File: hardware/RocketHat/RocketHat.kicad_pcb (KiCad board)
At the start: 4 copper layers, 28 x 25 mm, 2 parts, among them J1 Conn_02x16_Top_Bottom, J2 Conn_02x16_Top_Bottom

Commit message: Rocket hat sensor libraries
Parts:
- added U1: BMP390, bmp390:10LGA_2X2X0p75_BOS, F.Cu at (152.5, 117.7)
- added U2: BMI088, Package_LGA:Bosch_LGA-16_4.5x3mm_P0.5mm_LayoutBorder7x1y_ClockwisePinNumbering, F.Cu at (152.7, 113.5)
- added U3: ADXL375BCCZ, adxl375:LGA_CC-14-1_ADI, F.Cu at (134.5, 115.8)
- added U4: CAM-M8C-0, CAM-M8C-0:CAM-M8C-0, F.Cu at (143.0, 103.5)

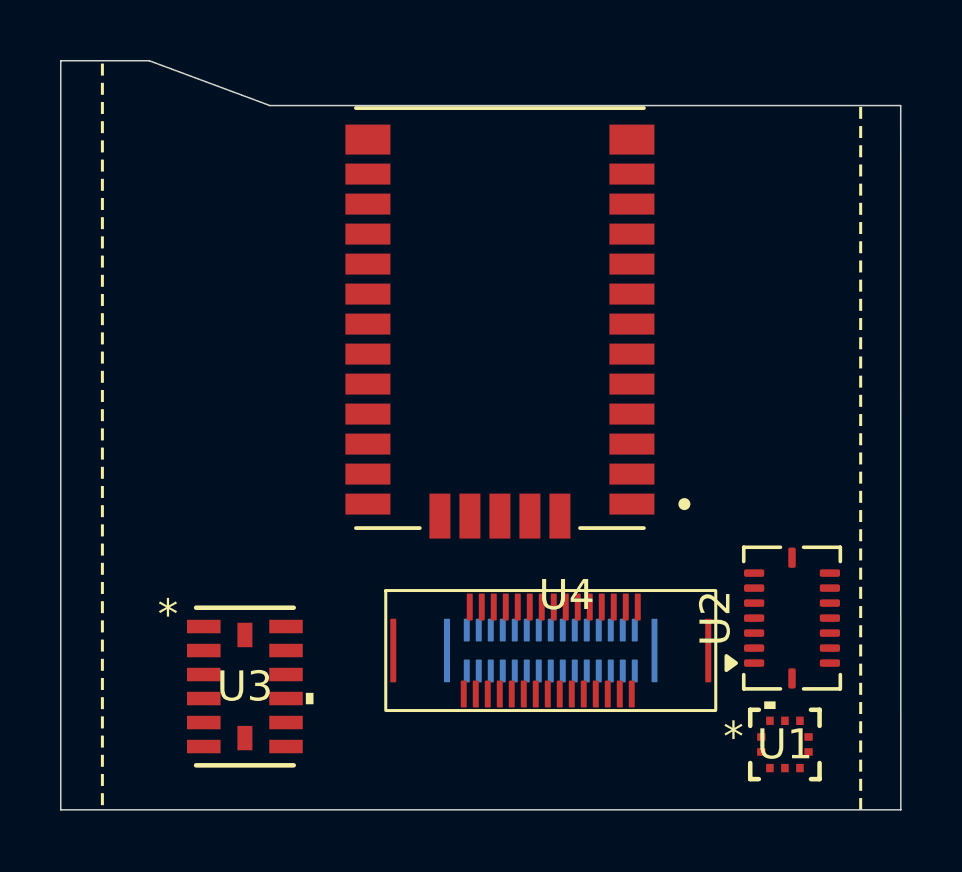
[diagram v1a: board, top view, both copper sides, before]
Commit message: Rocket Hat schematic done
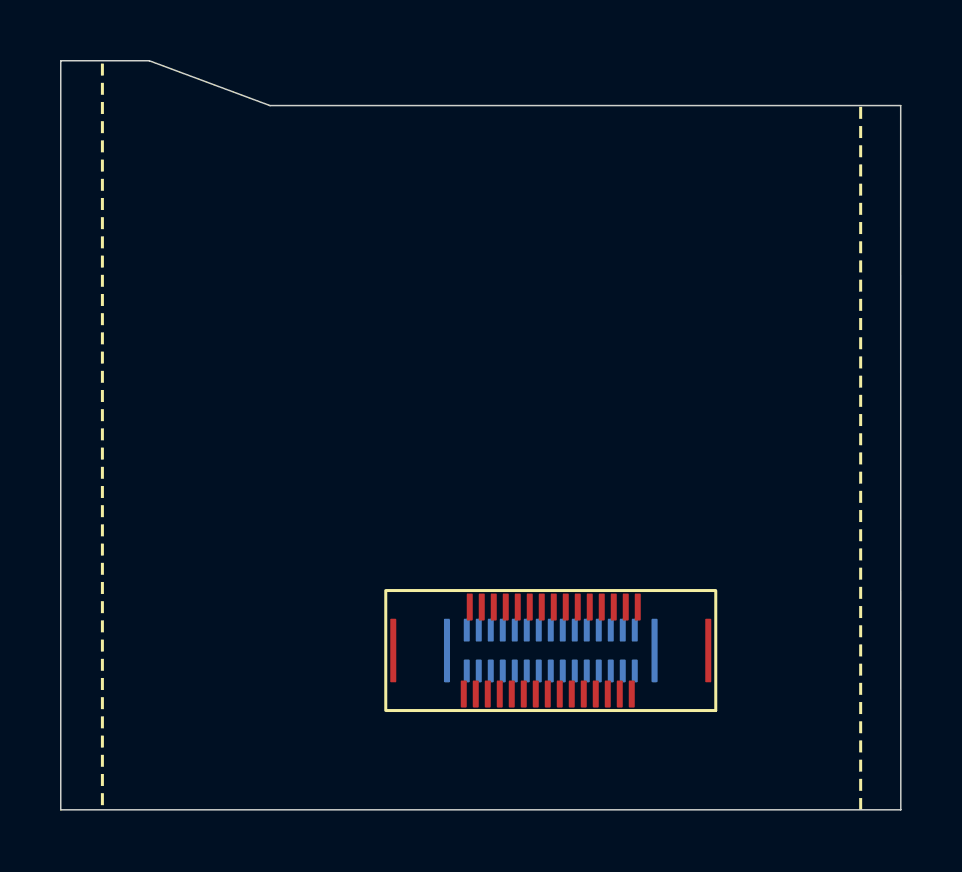
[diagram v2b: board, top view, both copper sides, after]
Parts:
- removed U1: BMP390, bmp390:10LGA_2X2X0p75_BOS
- removed U2: BMI088, Package_LGA:Bosch_LGA-16_4.5x3mm_P0.5mm_LayoutBorder7x1y_ClockwisePinNumbering
- removed U3: ADXL375BCCZ, adxl375:LGA_CC-14-1_ADI
- removed U4: CAM-M8C-0, CAM-M8C-0:CAM-M8C-0
- turned J2 to 180 degrees
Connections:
- J1 pad 17: CONN_16 -> CONN_16/I4
- J1 pad 18: CONN_17 -> CONN_17/I3
- J1 pad 19: CONN_18 -> CONN_18/I2
- J1 pad 20: CONN_19 -> CONN_19/I1
- J1 pad 21: CONN_20 -> CONN_20/I0
- J1 pad 22: CONN_21 -> CONN_21/RESP
- J2 pad 1: CONN_15 -> CONN_14
- J2 pad 10: CONN_24 -> CONN_5
- J2 pad 11: CONN_25 -> CONN_4
- J2 pad 12: CONN_26 -> CONN_3
- J2 pad 13: CONN_27 -> CONN_2
- J2 pad 14: CONN_28 -> CONN_1
- J2 pad 15: CONN_29 -> CONN_0
- J2 pad 16: CONN_0 -> CONN_29
- J2 pad 17: CONN_1 -> CONN_28
- J2 pad 18: CONN_2 -> CONN_27
- J2 pad 19: CONN_3 -> CONN_26
- J2 pad 2: CONN_16 -> CONN_13
- J2 pad 20: CONN_4 -> CONN_25
- J2 pad 21: CONN_5 -> CONN_24
- J2 pad 22: CONN_6 -> CONN_23
- J2 pad 23: CONN_7 -> CONN_22
- J2 pad 24: CONN_8 -> CONN_21
- J2 pad 25: CONN_9 -> CONN_20
- J2 pad 26: CONN_10 -> CONN_19
- J2 pad 27: CONN_11 -> CONN_18
- J2 pad 28: CONN_12 -> CONN_17
- J2 pad 29: CONN_13 -> CONN_16
- J2 pad 3: CONN_17 -> CONN_12
- J2 pad 30: CONN_14 -> CONN_15
- J2 pad 4: CONN_18 -> CONN_11
- J2 pad 5: CONN_19 -> CONN_10
- J2 pad 6: CONN_20 -> CONN_9
- J2 pad 7: CONN_21 -> CONN_8
- J2 pad 8: CONN_22 -> CONN_7
- J2 pad 9: CONN_23 -> CONN_6

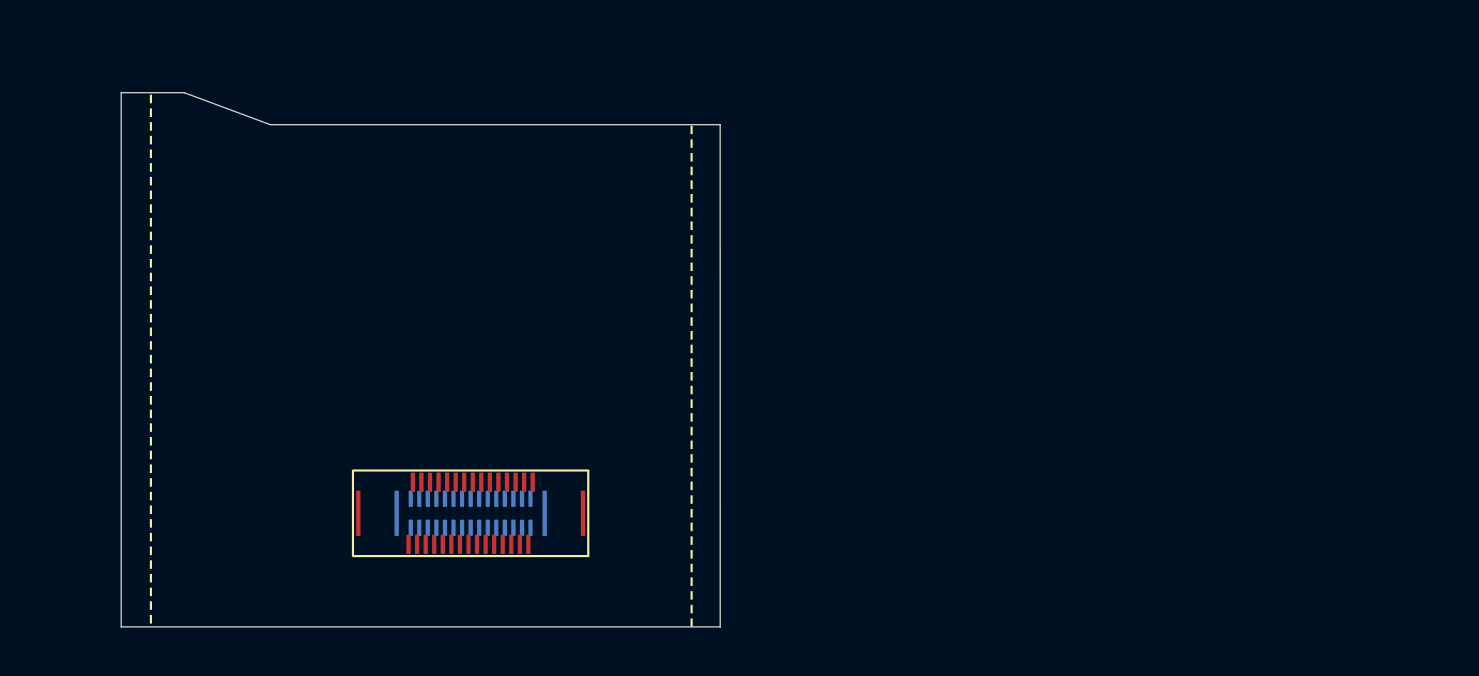
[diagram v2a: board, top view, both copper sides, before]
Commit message: rocket hat footprints done
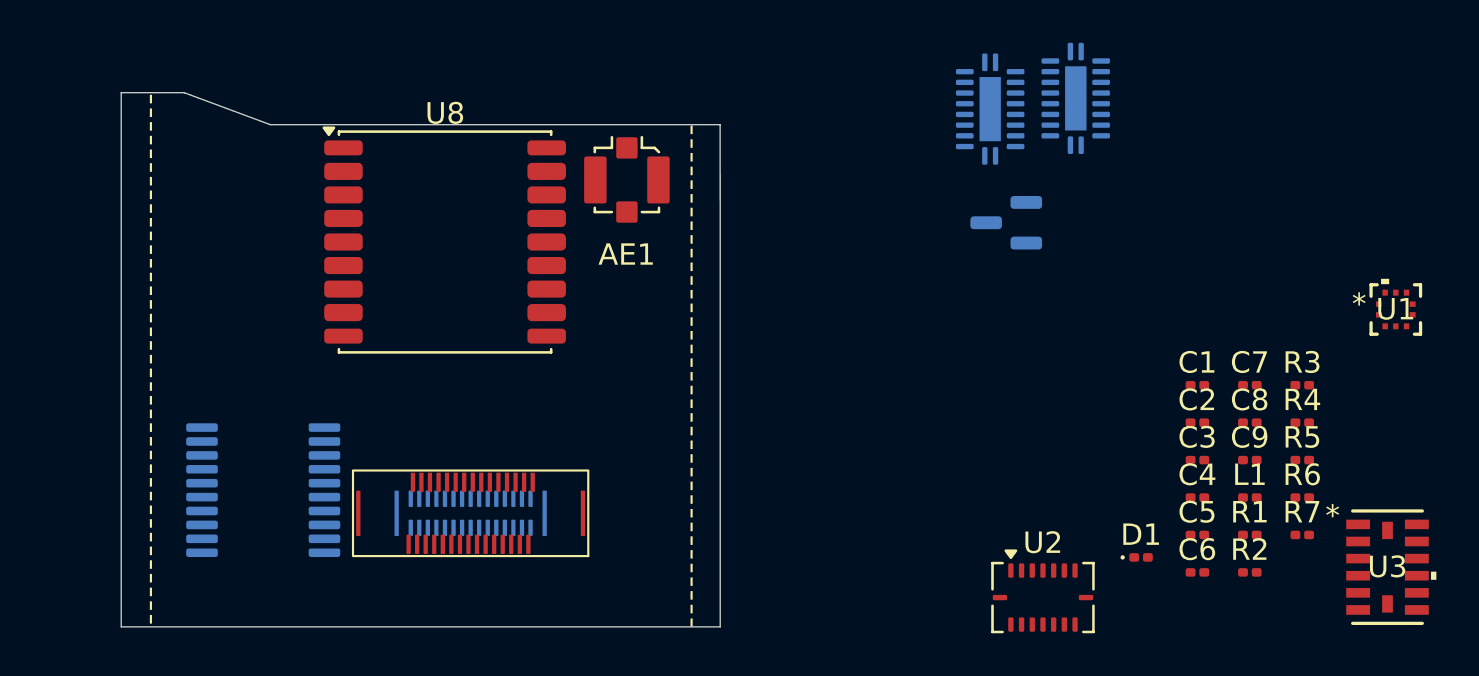
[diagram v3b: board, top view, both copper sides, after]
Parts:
- added AE1: Antenna_Shield, Connector_Coaxial:U.FL_Molex_MCRF_73412-0110_Vertical, F.Cu at (152.0, 99.0)
- added C1: 100nF, Capacitor_SMD:C_0201_0603Metric, F.Cu at (178.7, 108.6)
- added C2: 100nF, Capacitor_SMD:C_0201_0603Metric, F.Cu at (178.7, 110.3)
- added C3: 100nF, Capacitor_SMD:C_0201_0603Metric, F.Cu at (178.7, 112.1)
- added C4: 100nF, Capacitor_SMD:C_0201_0603Metric, F.Cu at (178.7, 113.8)
- added C5: 100nF, Capacitor_SMD:C_0201_0603Metric, F.Cu at (178.7, 115.6)
- added C6: 100nF, Capacitor_SMD:C_0201_0603Metric, F.Cu at (178.7, 117.3)
- added C7: 100nF, Capacitor_SMD:C_0201_0603Metric, F.Cu at (181.1, 108.6)
- added C8: 100nF, Capacitor_SMD:C_0201_0603Metric, F.Cu at (181.1, 110.3)
- added C9: 10 nF, Capacitor_SMD:C_0201_0603Metric, F.Cu at (181.1, 112.1)
- added D1: BLUE LED, LED_SMD:LED_0201_0603Metric, F.Cu at (176.0, 116.6)
- added L1: 27 nH, Inductor_SMD:L_0201_0603Metric, F.Cu at (181.1, 113.8)
- added Q2: MMBT2222A, Package_TO_SOT_SMD:SOT-23, B.Cu at (169.7, 101.0)
- added R1: 1k, Resistor_SMD:R_0201_0603Metric, F.Cu at (181.1, 115.6)
- added R2: 1k, Resistor_SMD:R_0201_0603Metric, F.Cu at (181.1, 117.3)
- added R3: 10k, Resistor_SMD:R_0201_0603Metric, F.Cu at (183.6, 108.6)
- added R4: 10k, Resistor_SMD:R_0201_0603Metric, F.Cu at (183.6, 110.3)
- added R5: 10k, Resistor_SMD:R_0201_0603Metric, F.Cu at (183.6, 112.1)
- added R6: 300, Resistor_SMD:R_0201_0603Metric, F.Cu at (183.6, 113.8)
- added R7: 10, Resistor_SMD:R_0201_0603Metric, F.Cu at (183.6, 115.6)
- added U1: BMP390, bmp390:10LGA_2X2X0p75_BOS, F.Cu at (187.9, 105.1)
- added U2: BMI088, Package_LGA:Bosch_LGA-16_4.5x3mm_P0.5mm_LayoutBorder7x1y_ClockwisePinNumbering, F.Cu at (171.4, 118.5)
- added U3: ADXL375BCCZ, adxl375:LGA_CC-14-1_ADI, F.Cu at (187.6, 117.1)
- added U5: 74HC688, Package_SO:TSSOP-20_4.4x6.5mm_P0.65mm, B.Cu at (135.0, 113.5)
- added U6: 74HC245, Package_DFN_QFN:DHVQFN-20-1EP_2.5x4.5mm_P0.5mm_EP1x3mm, B.Cu at (173.0, 95.2)
- added U7: 74HC245, Package_DFN_QFN:DHVQFN-20-1EP_2.5x4.5mm_P0.5mm_EP1x3mm, B.Cu at (169.0, 95.7)
- added U8: MAX-M10S, RF_GPS:ublox_MAX, F.Cu at (143.5, 101.9)
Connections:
- J1 pad 31: VIN -> GND
- J2 pad 31: VIN -> GND

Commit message: rocket hat connector labels
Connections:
- net CONN_0 renamed CONN_0/D0
- net CONN_1 renamed CONN_1/D1
- net CONN_10 renamed CONN_10/D13
- net CONN_11 renamed CONN_11/D12
- net CONN_12 renamed CONN_12/D11
- net CONN_13 renamed CONN_13/D10
- net CONN_14 renamed CONN_14/D9
- net CONN_2 renamed CONN_2/D2
- net CONN_28 renamed CONN_28/D15
- net CONN_29 renamed CONN_29/D14
- net CONN_3 renamed CONN_3/D3
- net CONN_4 renamed CONN_4/D4
- net CONN_5 renamed CONN_5/D5
- net CONN_6 renamed CONN_6/D6
- net CONN_7 renamed CONN_7/D7
- net CONN_8 renamed CONN_8/D8
- AE1 pad 2: GND -> CONN_26/GND
- C1 pad 1: +3V3 -> CONN_20/3V3
- C1 pad 2: GND -> CONN_26/GND
- C2 pad 1: +3V3 -> CONN_20/3V3
- C2 pad 2: GND -> CONN_26/GND
- C3 pad 1: GND -> CONN_26/GND
- C3 pad 2: +3V3 -> CONN_20/3V3
- C4 pad 1: GND -> CONN_26/GND
- C4 pad 2: +3V3 -> CONN_20/3V3
- C5 pad 1: +3V3 -> CONN_20/3V3
- C5 pad 2: GND -> CONN_26/GND
- C6 pad 1: +3V3 -> CONN_20/3V3
- C6 pad 2: GND -> CONN_26/GND
- C7 pad 1: GND -> CONN_26/GND
- C7 pad 2: +3V3 -> CONN_20/3V3
- C8 pad 1: GND -> CONN_26/GND
- C8 pad 2: +3V3 -> CONN_20/3V3
- C9 pad 2: GND -> CONN_26/GND
- J1 pad 10: CONN_9 -> CONN_9/RESP
- J1 pad 16: CONN_15 -> CONN_15/I4
- J1 pad 17: CONN_16/I4 -> CONN_16/I3
- J1 pad 18: CONN_17/I3 -> CONN_17/I2
- J1 pad 19: CONN_18/I2 -> CONN_18/I1
- J1 pad 20: CONN_19/I1 -> CONN_19/I0
- J1 pad 21: CONN_20/I0 -> CONN_20/3V3
- J1 pad 22: CONN_21/RESP -> CONN_20/3V3
- J1 pad 23: CONN_22 -> CONN_20/3V3
- J1 pad 24: CONN_23 -> CONN_23/5V
- J1 pad 25: CONN_24 -> CONN_23/5V
- J1 pad 26: CONN_25 -> CONN_23/5V
- J1 pad 27: CONN_26 -> CONN_26/GND
- J1 pad 28: CONN_27 -> CONN_26/GND
- J1 pad 31: GND -> CONN_26/GND
- J1 pad 32: GND -> CONN_26/GND
- J2 pad 18: CONN_27 -> CONN_26/GND
- J2 pad 19: CONN_26 -> CONN_26/GND
- J2 pad 20: CONN_25 -> CONN_23/5V
- J2 pad 21: CONN_24 -> CONN_23/5V
- J2 pad 22: CONN_23 -> CONN_23/5V
- J2 pad 23: CONN_22 -> CONN_20/3V3
- J2 pad 24: CONN_21 -> CONN_20/3V3
- J2 pad 25: CONN_20 -> CONN_20/3V3
- J2 pad 26: CONN_19 -> CONN_19/I0
- J2 pad 27: CONN_18 -> CONN_18/I1
- J2 pad 28: CONN_17 -> CONN_17/I2
- J2 pad 29: CONN_16 -> CONN_16/I3
- J2 pad 30: CONN_15 -> CONN_15/I4
- J2 pad 31: GND -> CONN_26/GND
- J2 pad 32: GND -> CONN_26/GND
- J2 pad 6: CONN_9 -> CONN_9/RESP
- Q2 pad 2: GND -> CONN_26/GND
- R2 pad 2: +3V3 -> CONN_23/5V
- R3 pad 2: +3V3 -> CONN_20/3V3
- R4 pad 2: +3V3 -> CONN_20/3V3
- R5 pad 2: +3V3 -> CONN_20/3V3
- R6 pad 1: CONN_21/RESP -> CONN_9/RESP
- U1 pad 1: +3V3 -> CONN_20/3V3
- U1 pad 10: +3V3 -> CONN_20/3V3
- U1 pad 3: GND -> CONN_26/GND
- U1 pad 8: GND -> CONN_26/GND
- U1 pad 9: GND -> CONN_26/GND
- U2 pad 11: +3V3 -> CONN_20/3V3
- U2 pad 2: GND -> CONN_26/GND
- U2 pad 3: +3V3 -> CONN_20/3V3
- U2 pad 4: GND -> CONN_26/GND
- U2 pad 6: GND -> CONN_26/GND
- U2 pad 7: GND -> CONN_26/GND
- U3 pad 1: +3V3 -> CONN_20/3V3
- U3 pad 2: GND -> CONN_26/GND
- U3 pad 4: GND -> CONN_26/GND
- U3 pad 5: GND -> CONN_26/GND
- U3 pad 6: +3V3 -> CONN_20/3V3
- U5 pad 1: GND -> CONN_26/GND
- U5 pad 10: GND -> CONN_26/GND
- U5 pad 11: CONN_16/I4 -> CONN_15/I4
- U5 pad 12: GND -> CONN_26/GND
- U5 pad 13: GND -> CONN_26/GND
- U5 pad 14: GND -> CONN_26/GND
- U5 pad 15: GND -> CONN_26/GND
- U5 pad 16: GND -> CONN_26/GND
- U5 pad 17: GND -> CONN_26/GND
- U5 pad 18: GND -> CONN_26/GND
- U5 pad 2: CONN_20/I0 -> CONN_19/I0
- U5 pad 20: +3V3 -> CONN_23/5V
- U5 pad 3: GND -> CONN_26/GND
- U5 pad 4: CONN_19/I1 -> CONN_18/I1
- U5 pad 5: +3V3 -> CONN_23/5V
- U5 pad 6: CONN_18/I2 -> CONN_17/I2
- U5 pad 7: GND -> CONN_26/GND
- U5 pad 8: CONN_17/I3 -> CONN_16/I3
- U5 pad 9: GND -> CONN_26/GND
- U6 pad 1: +3V3 -> CONN_23/5V
- U6 pad 10: GND -> CONN_26/GND
- U6 pad 20: +3V3 -> CONN_23/5V
- U7 pad 1: +3V3 -> CONN_23/5V
- U7 pad 10: GND -> CONN_26/GND
- U7 pad 20: +3V3 -> CONN_23/5V
- U8 pad 1: GND -> CONN_26/GND
- U8 pad 10: GND -> CONN_26/GND
- U8 pad 12: GND -> CONN_26/GND
- U8 pad 7: +3V3 -> CONN_20/3V3
- U8 pad 8: +3V3 -> CONN_20/3V3

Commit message: start routing
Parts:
- C4, D1, R6: moved to B.Cu
- moved U1 54.5 mm to (133.7, 99.8)
- moved R6 54.2 mm to (132.1, 96.9), turned to 90 degrees
- moved U3 53.3 mm to (134.5, 112.9)
- moved D1 49.7 mm to (130.8, 96.0), turned to 180 degrees
- moved C2 47.8 mm to (131.9, 100.4), turned to -90 degrees
- moved C1 46.4 mm to (133.5, 98.0)
- moved C4 44.7 mm to (134.5, 106.7), turned to 180 degrees
- moved Q2 43.9 mm to (126.2, 107.2), turned to -90 degrees
- moved C3 42.4 mm to (136.8, 105.7), turned to 90 degrees
- moved U2 39.0 mm to (134.5, 105.9), turned to -90 degrees
- moved U7 30.4 mm to (141.8, 109.3), turned to -90 degrees
- moved U6 28.9 mm to (147.8, 109.3), turned to 90 degrees
- moved C7 20.3 mm to (162.1, 101.6)
- moved C8 20.3 mm to (162.1, 103.3)
- moved C9 20.3 mm to (162.1, 105.1)
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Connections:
- U6 pad 21: (no net) -> CONN_26/GND
- U7 pad 21: (no net) -> CONN_26/GND
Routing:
- net CONN_23/5V: track 0.00 -> 52.5 mm, vias 0 -> 7
- net CONN_26/GND: track 0.00 -> 48.5 mm, vias 0 -> 13
- net Net-(U5-P=R): track 0.00 -> 23.2 mm, vias 0 -> 2
- net CONN_20/3V3: track 0.00 -> 20.5 mm, vias 0 -> 9
- net CONN_16/I3: track 0.00 -> 17.6 mm, vias 0 -> 1
- net CONN_15/I4: track 0.00 -> 17.4 mm, vias 0 -> 1
- net CONN_17/I2: track 0.00 -> 17.3 mm, vias 0 -> 1
- net CONN_18/I1: track 0.00 -> 17.0 mm, vias 0 -> 1
- net CONN_19/I0: track 0.00 -> 16.8 mm, vias 0 -> 2
- net CONN_28/D15: track 0.00 -> 15.7 mm, vias 0 -> 2
- net CONN_29/D14: track 0.00 -> 13.8 mm, vias 0 -> 2
- net CONN_8/D8: track 0.00 -> 12.8 mm, vias 0 -> 1
- net CONN_0/D0: track 0.00 -> 9.59 mm, vias 0 -> 2
- net CONN_1/D1: track 0.00 -> 9.51 mm, vias 0 -> 2
- net CONN_14/D9: track 0.00 -> 8.99 mm, vias 0 -> 2
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- added copper zone on In2.Cu, net CONN_20/3V3
- added copper zone on In1.Cu, net CONN_26/GND

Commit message: Work more on traces for rocket hat and add dipswitch
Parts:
- added R8: 10k, Resistor_SMD:R_0201_0603Metric, F.Cu at (153.0, 111.6)
- added SW1: SW_DIP_x01, Button_Switch_SMD:SW_DIP_SPSTx01_Slide_Copal_CHS-01A_W5.08mm_P1.27mm_JPin, F.Cu at (153.0, 116.0)
- moved C6 28.0 mm to (131.9, 114.2), turned to 90 degrees
- moved C5 27.9 mm to (131.9, 111.3), turned to -90 degrees
- moved C7 25.8 mm to (136.3, 100.6), turned to -90 degrees
- moved C8 25.0 mm to (137.2, 100.6), turned to -90 degrees
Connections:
- U5 pad 5: CONN_23/5V -> Net-(U5-R1)
- U7 pad 21: CONN_26/GND -> (no net)
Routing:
- net CONN_26/GND: track 48.5 -> 67.0 mm, vias 13 -> 15
- net CONN_20/3V3: track 20.5 -> 37.1 mm, vias 9 -> 11
- net Net-(U5-R1): track 0.00 -> 1.54 mm

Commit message: keep routing rocket hat
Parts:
- moved R1 36.2 mm to (125.9, 110.3)
- moved R2 36.2 mm to (125.9, 112.0)
- moved R3 20.5 mm to (145.2, 108.5), turned to 90 degrees
- moved R4 19.3 mm to (145.9, 108.5), turned to 90 degrees
- moved R5 18.3 mm to (146.6, 108.5), turned to 90 degrees
- moved R7 15.8 mm to (150.2, 101.9)
- moved C9 12.1 mm to (150.2, 103.0), turned to 180 degrees
- moved L1 11.5 mm to (151.7, 101.9)
- moved U6 4.77 mm to (152.3, 108.0), turned to 0 degrees
- moved U7 0.10 mm to (141.8, 109.5)
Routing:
- net D12/ACCEL_HIGH: track 0.00 -> 36.1 mm, vias 0 -> 1
- net Net-(U5-R1): track 1.54 -> 31.6 mm, vias 0 -> 1
- net D10/GPS_RX: track 0.00 -> 28.0 mm, vias 0 -> 3
- net D11/GPS_TX: track 0.00 -> 24.3 mm, vias 0 -> 5
- net CONN_26/GND: track 67.0 -> 81.6 mm, vias 15 -> 22
- net Net-(AE1-A): track 0.00 -> 7.56 mm
- net CONN_12/D11: track 8.82 -> 16.3 mm
- net D2/SDO: track 0.00 -> 7.41 mm, vias 0 -> 1
- net CONN_10/D13: track 5.13 -> 12.2 mm, vias 1 -> 2
- net D0/SCL: track 0.00 -> 6.95 mm, vias 0 -> 1
- net D1/SDI: track 0.00 -> 6.83 mm, vias 0 -> 1
- net CONN_11/D12: track 5.25 -> 11.5 mm, vias 1 -> 2
- net CONN_13/D10: track 5.41 -> 10.5 mm, vias 1 -> 3
- net CONN_23/5V: track 52.5 -> 47.6 mm, vias 7 -> 8
- net CONN_14/D9: track 8.99 -> 13.0 mm
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
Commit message: rocker hat work
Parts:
- R1, R2: moved to B.Cu
- turned R1 to 180 degrees
- turned R2 to 180 degrees
